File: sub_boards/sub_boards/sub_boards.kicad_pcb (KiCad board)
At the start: 2 copper layers, 16 parts, among them J1 Raspberry_Pi_5, J3 2.54mm PinHeader, J4 2.54mm PinHeader, Q1 ST-1KL3A, Q2 ST-1KL3A, Q3 ST-1KL3A, Q4 ST-1KL3A, SW1 TVBP06-B043CB-B, SW2 TVBP06-B043CB-B, SW3 TVBP06-B043CB-B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

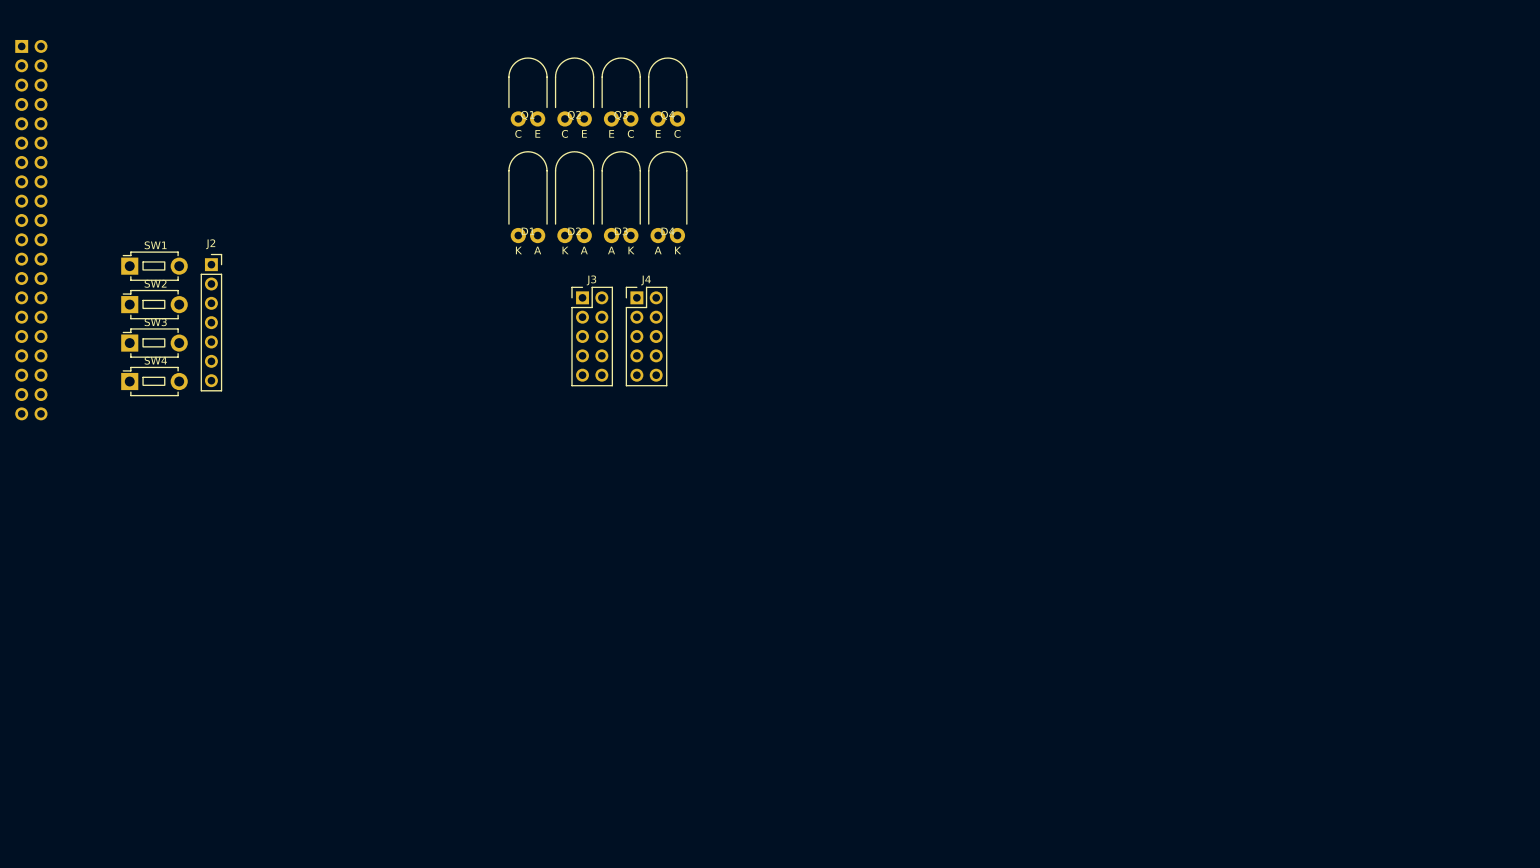
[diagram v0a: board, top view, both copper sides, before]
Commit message: サブ基板アートワーク完了
Signed-off-by: Kazuki Iida <elkel53930@gmail.com>
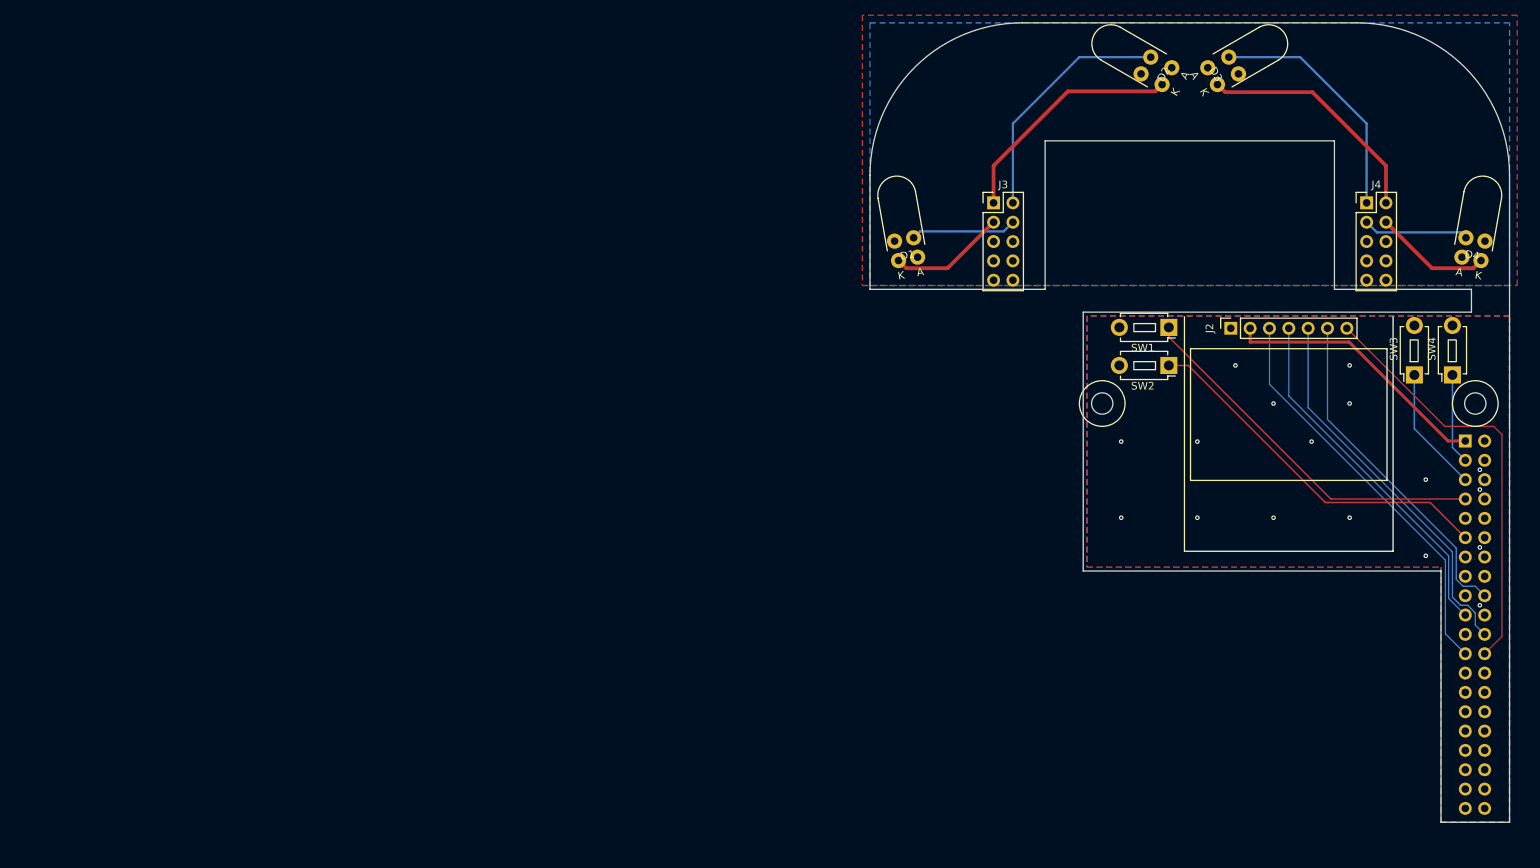
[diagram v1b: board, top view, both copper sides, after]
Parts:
- added H1: MountingHole, Library:M2.6 Mounting Hole, F.Cu at (210.5, 85.0)
- added H2: MountingHole, Library:M2.6 Mounting Hole, F.Cu at (259.5, 85.0)
- Q1, Q2, Q3, Q4: moved to B.Cu
- moved J1 196.6 mm to (258.2, 89.9)
- moved SW4 173.7 mm to (256.5, 81.2), turned to 90 degrees
- moved SW3 168.8 mm to (251.5, 81.2), turned to 90 degrees
- moved SW1 136.7 mm to (219.2, 75.0), turned to 180 degrees
- moved SW2 136.7 mm to (219.2, 80.0), turned to 180 degrees
- moved J2 134.2 mm to (227.4, 75.1), turned to 90 degrees
- moved Q4 106.7 mm to (259.0, 66.4), turned to 170 degrees
- moved D4 105.6 mm to (259.0, 66.0), turned to -10 degrees
- moved J4 96.7 mm to (245.2, 58.6)
- moved D2 80.6 mm to (219.0, 42.0), turned to 60 degrees
- moved D3 80.5 mm to (225.0, 42.0), turned to -60 degrees
- moved Q3 78.3 mm to (225.2, 42.1), turned to 120 degrees
- moved Q2 78.1 mm to (218.8, 42.1), turned to -120 degrees
- moved J3 55.4 mm to (196.2, 58.6)
- moved Q1 52.4 mm to (185.0, 66.4), turned to -170 degrees
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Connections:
- J1 pad 11: unconnected-(J1-GPIO17/SPI1_~{CE1}-Pad11) -> /BTN_UP
- J1 pad 14: unconnected-(J1-GND-Pad14) -> GND
- J1 pad 20: unconnected-(J1-GND-Pad20) -> GND
- J1 pad 25: unconnected-(J1-GND-Pad25) -> GND
- J1 pad 3: unconnected-(J1-SDA_I2C1/GPIO02-Pad3) -> /BTN_LEFT
- J1 pad 30: unconnected-(J1-GND-Pad30) -> GND
- J1 pad 34: unconnected-(J1-GND-Pad34) -> GND
- J1 pad 35: /BTN_DOWN -> unconnected-(J1-GPIO19/SPI1_MISO/PCM_FS-Pad35)
- J1 pad 36: /BTN_RIGHT -> unconnected-(J1-GPIO16/SPI1_~{CE2}-Pad36)
- J1 pad 37: /BTN_UP -> unconnected-(J1-GPIO26/SDIO_DAT2-Pad37)
- J1 pad 38: /BTN_LEFT -> unconnected-(J1-GPIO20/SPI1_MOSI/PCM_DIN/PWM1-Pad38)
- J1 pad 39: unconnected-(J1-GND-Pad39) -> GND
- J1 pad 5: unconnected-(J1-SCL_I2C1/GPIO03-Pad5) -> /BTN_RIGHT
- J1 pad 7: unconnected-(J1-GPCLK0/GPIO04-Pad7) -> /BTN_DOWN
- J1 pad 9: unconnected-(J1-GND-Pad9) -> GND
- SW1 pad 1: /BTN_UP -> /BTN_DOWN
- SW2 pad 1: /BTN_DOWN -> /BTN_UP
- SW3 pad 1: /BTN_LEFT -> /BTN_RIGHT
- SW4 pad 1: /BTN_RIGHT -> /BTN_LEFT
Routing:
- net /CS: track 0.00 -> 55.9 mm
- net /SCLK: track 0.00 -> 53.4 mm
- net /RES: track 0.00 -> 50.3 mm
- net /BTN_DOWN: track 0.00 -> 49.0 mm
- net /BTN_UP: track 0.00 -> 48.3 mm
- net /MOSI: track 0.00 -> 47.3 mm
- net /DC: track 0.00 -> 44.6 mm
- net +3.3V: track 0.00 -> 35.5 mm
- net /RS_PHTR: track 0.00 -> 32.1 mm
- net /LS_PHTR: track 0.00 -> 32.1 mm
- net /RS_LED: track 0.00 -> 31.4 mm
- net /LS_LED: track 0.00 -> 31.4 mm
- net /BTN_RIGHT: track 0.00 -> 16.5 mm
- net /LF_LED: track 0.00 -> 15.4 mm
- net /RF_LED: track 0.00 -> 15.4 mm
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- added copper zone on B.Cu, net /SEN_3V3
- added copper zone on F.Cu, net /SEN_5V
- added copper zone on B.Cu, net GND
- added copper zone on F.Cu, net GND
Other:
- board outline added: 84 x 105 mm

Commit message: アートワーク微修正
Signed-off-by: Kazuki Iida <elkel53930@gmail.com>
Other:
- outline, holes or cut-outs redrawn
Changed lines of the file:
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@@
 		(tags "PHAP3362 6mm tact sw THT")
 		(property "Reference" "SW2"
-			(at 3.42 -2.7 0)
+			(at 3.25 0 0)
 			(layer "F.SilkS")
 			(effects
@@
 		)
 		(fp_text user "${REFERENCE}"
-			(at 3 0 0)
+			(at 3 0 180)
 			(layer "F.Fab")
 			(effects
@@
 		(tags "PHAP3362 6mm tact sw THT")
 		(property "Reference" "SW4"
-			(at 3.42 -2.7 90)
+			(at 3.25 0 90)
 			(layer "F.SilkS")
 			(effects
@@
 		(at 219 42 60)
 		(property "Reference" "D2"
-			(at 0 -0.5 60)
+			(at -0.084936 -5.147114 60)
 			(unlocked yes)
 			(layer "F.SilkS")
@@
 		(tags "PHAP3362 6mm tact sw THT")
 		(property "Reference" "SW3"
-			(at 3.42 -2.7 90)
+			(at 3.25 0 90)
 			(layer "F.SilkS")
 			(effects
@@
 		(at 185 66 10)
 		(property "Reference" "D1"
-			(at 0 -0.5 10)
+			(at -0.203391 -4.605283 10)
 			(unlocked yes)
 			(layer "F.SilkS")
@@
 		(at 225 42 -60)
 		(property "Reference" "D3"
-			(at 0 -0.5 300)
+			(at 0.084936 -5.147114 300)
 			(unlocked yes)
 			(layer "F.SilkS")
@@
 		(tags "PHAP3362 6mm tact sw THT")
 		(property "Reference" "SW1"
-			(at 3.42 -2.7 0)
+			(at 3.25 0 0)
 			(layer "F.SilkS")
 			(effects
@@
 		(at 259 66 -10)
 		(property "Reference" "D4"
-			(at 0 -0.5 350)
+			(at 0.203391 -4.605283 350)
 			(unlocked yes)
 			(layer "F.SilkS")
@@
 		(at 259 66.405 170)
 		(property "Reference" "Q4"
-			(at 0 3.5 350)
+			(at 3.632519 3.32473 350)
 			(unlocked yes)
 			(layer "B.SilkS")
@@
 		)
 		(fp_text user "C"
-			(at 1.27 1 350)
+			(at 0.938568 5.322886 350)
 			(unlocked yes)
 			(layer "B.SilkS")
@@
 		)
 		(fp_text user "E"
-			(at -1.27 1 350)
+			(at -1.610275 5.264602 350)
 			(unlocked yes)
 			(layer "B.SilkS")
@@
 		(at 185 66.405 -170)
 		(property "Reference" "Q1"
-			(at 0 3.5 10)
+			(at -3.632519 3.32473 10)
 			(unlocked yes)
 			(layer "B.SilkS")
@@
 		)
 		(fp_text user "E"
-			(at 1.27 1 10)
+			(at 1.117871 5.177778 10)
 			(unlocked yes)
 			(layer "B.SilkS")
@@
 		)
 		(fp_text user "C"
-			(at -1.27 1 10)
+			(at -0.938568 5.322886 10)
 			(unlocked yes)
 			(layer "B.SilkS")
@@
 		(at 218.835608 42.105074 -120)
 		(property "Reference" "Q2"
-			(at 0 3.5 60)
+			(at 3.375845 3.057284 60)
 			(unlocked yes)
 			(layer "B.SilkS")
@@
 		)
 		(fp_text user "C"
-			(at -1.27 1 60)
+			(at -1.204282 5.124271 60)
 			(unlocked yes)
 			(layer "B.SilkS")
@@
 		)
 		(fp_text user "E"
-			(at 1.27 1 60)
+			(at 1.027769 4.990296 60)
 			(unlocked yes)
 			(layer "B.SilkS")
@@
 		(at 225.164392 42.105074 120)
 		(property "Reference" "Q3"
-			(at 0 3.5 300)
+			(at -3.375845 3.057284 300)
 			(unlocked yes)
 			(layer "B.SilkS")
@@
 		)
 		(fp_text user "E"
-			(at -1.27 1 300)
+			(at -1.027769 4.990296 300)
 			(unlocked yes)
 			(layer "B.SilkS")
@@
 		)
 		(fp_text user "C"
-			(at 1.27 1 300)
+			(at 1.204282 5.124271 300)
 			(unlocked yes)
 			(layer "B.SilkS")
@@
 	)
 	(gr_line
+		(start 255 70)
+		(end 264 70)
+		(stroke
+			(width 0.1)
+			(type default)
+		)
+		(layer "F.SilkS")
+	)
+	(gr_line
 		(start 221.3 73.6)
 		(end 221.3 104.4)
@@
 		(layer "F.SilkS")
 	)
+	(gr_line
+		(start 264 73)
+		(end 255 73)
+		(stroke
+			(width 0.1)
+			(type default)
+		)
+		(layer "F.SilkS")
+	)
 	(gr_curve
 		(pts
@@
 	)
 	(gr_line
-		(start 259 73)
-		(end 259 70)
+		(start 255 73)
+		(end 255 70)
 		(stroke
 			(width 0.05)
@@
 	(gr_line
 		(start 208 73)
-		(end 259 73)
+		(end 255 73)
 		(stroke
 			(width 0.05)
@@
 	)
 	(gr_line
-		(start 259 70)
+		(start 255 70)
 		(end 241 70)
 		(stroke

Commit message: 12/18 基板発注
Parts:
- added C15: CC0603KRX7R9BB104, Capacitor_SMD:C_0402_1005Metric, B.Cu at (257.0, 116.5)
- added C16: CL05B104KO5NNNC, Capacitor_SMD:C_0402_1005Metric, B.Cu at (239.0, 116.5)
- added H3: M2 mounting hole, MountingHole:MountingHole_2.2mm_M2, F.Cu at (255.5, 120.0)
- added H4: M2 mounting hole, MountingHole:MountingHole_2.2mm_M2, F.Cu at (255.5, 108.0)
- added H5: M2 mounting hole, MountingHole:MountingHole_2.2mm_M2, F.Cu at (237.5, 120.0)
- added H6: M2 mounting hole, MountingHole:MountingHole_2.2mm_M2, F.Cu at (237.5, 108.0)
- added J5: EncSide, Library:EncoderPad, B.Cu at (259.0, 114.0)
- added J6: EncSide, Library:EncoderPad, B.Cu at (241.0, 114.0)
- added J7: B2B-XH, Connector_JST:JST_XH_B2B-XH-AM_1x02_P2.50mm_Vertical, F.Cu at (186.0, 131.2)
- added U10: AS5047D, Package_SO:TSSOP-14_4.4x5mm_P0.65mm, F.Cu at (237.4, 114.0)
- added U9: AS5047D, Package_SO:TSSOP-14_4.4x5mm_P0.65mm, F.Cu at (255.5, 114.0)
- moved H2 77.7 mm to (195.5, 129.0)
- moved J1 72.5 mm to (194.2, 124.1), turned to 0 degrees
- moved SW1 66.6 mm to (202.2, 139.4)
- moved J2 63.8 mm to (227.6, 138.9), turned to -90 degrees
- moved SW2 57.9 mm to (202.2, 135.4)
- moved SW4 55.7 mm to (239.0, 134.1), turned to -90 degrees
- moved H1 55.6 mm to (244.5, 129.0)
- moved SW3 53.5 mm to (243.0, 134.1), turned to -90 degrees
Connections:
- J1 pad 11: /BTN_UP -> /BTN_RIGHT
- J1 pad 2: unconnected-(J1-5V-Pad2) -> /+5V
- J1 pad 3: /BTN_LEFT -> /BTN_DOWN
- J1 pad 4: unconnected-(J1-5V-Pad4) -> /+5V
- J1 pad 5: /BTN_RIGHT -> /BTN_UP
- J1 pad 7: /BTN_DOWN -> /BTN_LEFT
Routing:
- net /BTN_RIGHT: track 16.5 -> 64.6 mm, vias 0 -> 1
- net /BTN_LEFT: track 11.9 -> 55.1 mm, vias 0 -> 1
- net /BTN_DOWN: track 49.0 -> 27.2 mm, vias 0 -> 1
- net /BTN_UP: track 48.3 -> 28.7 mm, vias 0 -> 1
- net /RES: track 50.3 -> 65.9 mm, vias 0 -> 2
- net Net-(J5-Pin_2): track 0.00 -> 12.8 mm, vias 0 -> 1
- net Net-(J6-Pin_2): track 0.00 -> 12.8 mm, vias 0 -> 1
- net /DC: track 44.6 -> 56.4 mm
- net /+5V: track 0.00 -> 10.2 mm
- net /MOSI: track 47.3 -> 56.7 mm
- net Net-(J5-Pin_1): track 0.00 -> 9.20 mm, vias 0 -> 1
- net Net-(J6-Pin_1): track 0.00 -> 9.20 mm, vias 0 -> 1
- net /SCLK: track 53.4 -> 60.6 mm
- net Net-(J6-Pin_6): track 0.00 -> 7.11 mm, vias 0 -> 1
- net Net-(J5-Pin_6): track 0.00 -> 7.11 mm, vias 0 -> 1
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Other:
- board size 84 x 105 mm -> 84 x 108 mm
- board text added: "+5V"
- board text added: "GND"
